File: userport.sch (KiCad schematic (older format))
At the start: 25 parts, among them CN10 USERPORT, U122 74LS654, U21 74HCT04, U22 MOS_6529, U23 MOS_6551_ACIA, U28 GAL16V8, Y2 1.8432M

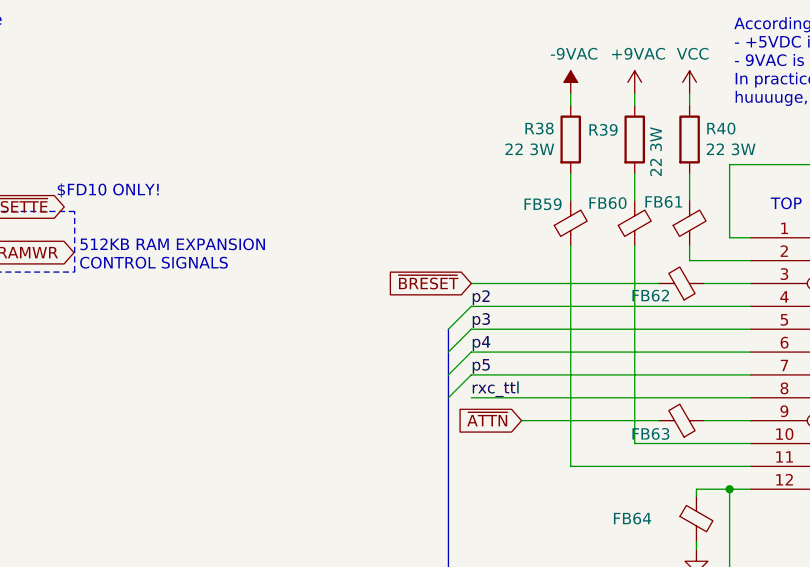
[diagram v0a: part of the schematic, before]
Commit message: Replace /BRESET on Expansion Port and User Port with /RESET This was an oversight we probably introduced in V3 which makes it impossible for the Expansion Port and User Port to reset the machine through the RESET pin. The /BRESET line only went to the IEC Port in the original machine, which means that "Serial button dongles" cannot reset the machine, unlike on the C64. Maybe we should introduce a jumper for that?
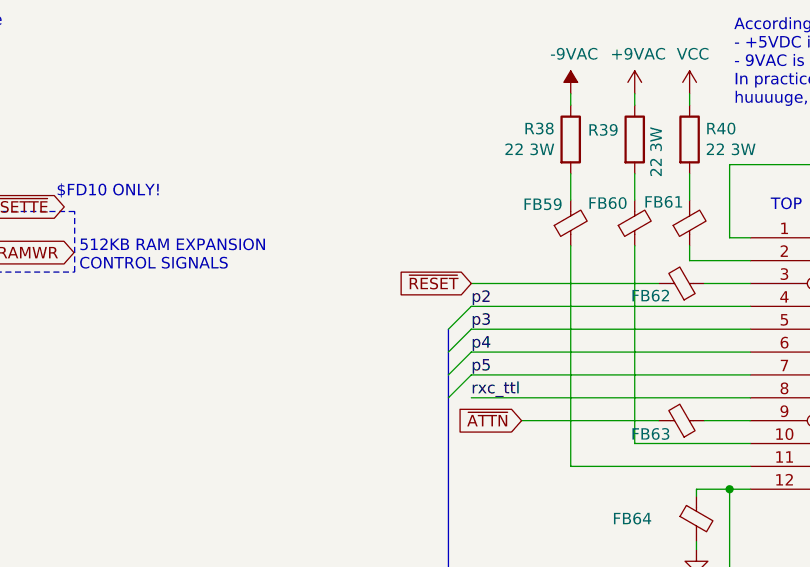
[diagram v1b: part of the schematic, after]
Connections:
- net ~BRESET is gone; now on net ~RESET: FB62.2
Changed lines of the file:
@@
 Sheet 13 14
 Title "LittleSixteen"
-Date "2023-02-14"
+Date "2024-07-21"
 Rev "4git"
 Comp "SukkoPera"
@@
 	2910 3125 2910 3365
 Text GLabel 6470 6730 0    50   Input ~ 0
-~BRESET
+~RESET
 $Comp
 L 74xx:74LS04 U21

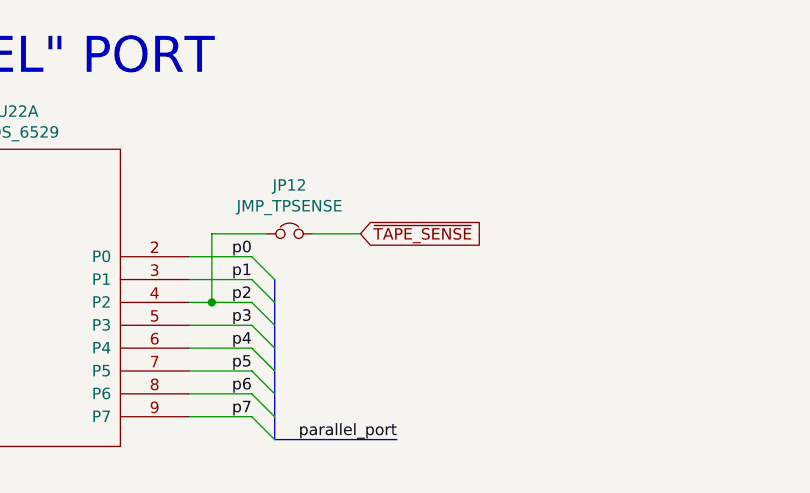
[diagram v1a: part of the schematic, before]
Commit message: Add P7 option for Tape Sense jumper, in order to replicate Plus/4 J8/J9
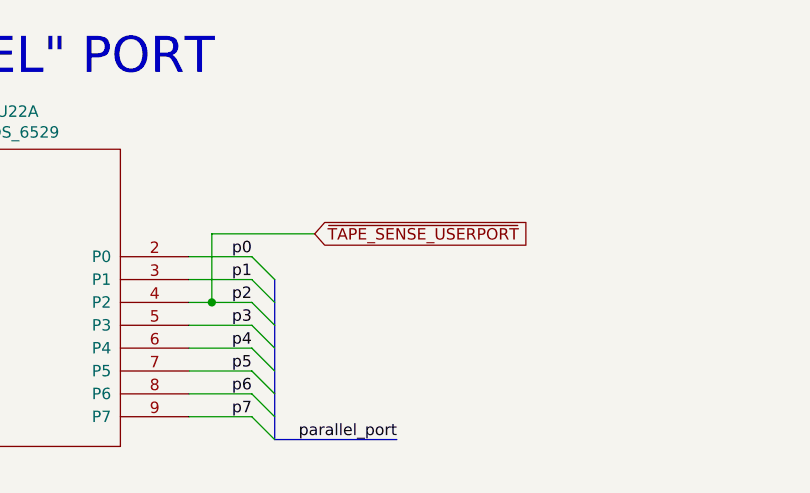
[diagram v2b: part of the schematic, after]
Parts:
- removed JP12: JMP_TPSENSE, Connector_PinHeader_2.54mm:PinHeader_1x02_P2.54mm_Vertical, symbol Device:Jumper_NC_Small
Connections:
- net p2 renamed ~TAPE_SENSE_USERPORT
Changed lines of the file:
@@
 Sheet 13 14
 Title "LittleSixteen"
-Date "2024-07-21"
+Date "2024-08-07"
 Rev "4git"
 Comp "SukkoPera"
@@
 Text GLabel 11775 1380 0    50   Input ~ 0
 R_~W
-Wire Wire Line
-	14150 1520 13940 1520
-$Comp
-L Device:Jumper_NC_Small JP?
-U 1 1 6486FE58
-P 13840 1520
-AR Path="/5E6A379E/6486FE58" Ref="JP?"  Part="1"
-AR Path="/63EAD078/6486FE58" Ref="JP12"  Part="1"
-F 0 "JP12" H 13840 1732 50  0000 C CNN
-F 1 "JMP_TPSENSE" H 13840 1641 50  0000 C CNN
-F 2 "Connector_PinHeader_2.54mm:PinHeader_1x02_P2.54mm_Vertical" H 13840 1520 50  0001 C CNN
-F 3 "~" H 13840 1520 50  0001 C CNN
-	1    13840 1520
-	-1   0    0    -1
-$EndComp
-Text GLabel 14150 1520 2    50   Input ~ 0
-~TAPE_SENSE
 $Comp
 L emi_filter_3pin:EMI_Filter_3Pin FB?
@@
 Wire Wire Line
 	13500 1520 13500 1820
-Wire Wire Line
-	13500 1520 13740 1520
 Connection ~ 13500 1820
 Wire Wire Line
@@
 Text Notes 1380 5695 0    50   ~ 0
 Generates:\n- Control signals for the Hannes RAM Expansion register at $FD16\n- ~CS~ for the User Port MOS 6529 (or replacement) at $FD10 only, named ~CASSETTE~ here\n- Other control signals for the User Port MOS 6529 replacement circuit
+Text GLabel 13950 1520 2    50   Input ~ 0
+~TAPE_SENSE_USERPORT
+Wire Wire Line
+	13500 1520 13950 1520
 Wire Bus Line
 	9765 6730 9765 8260

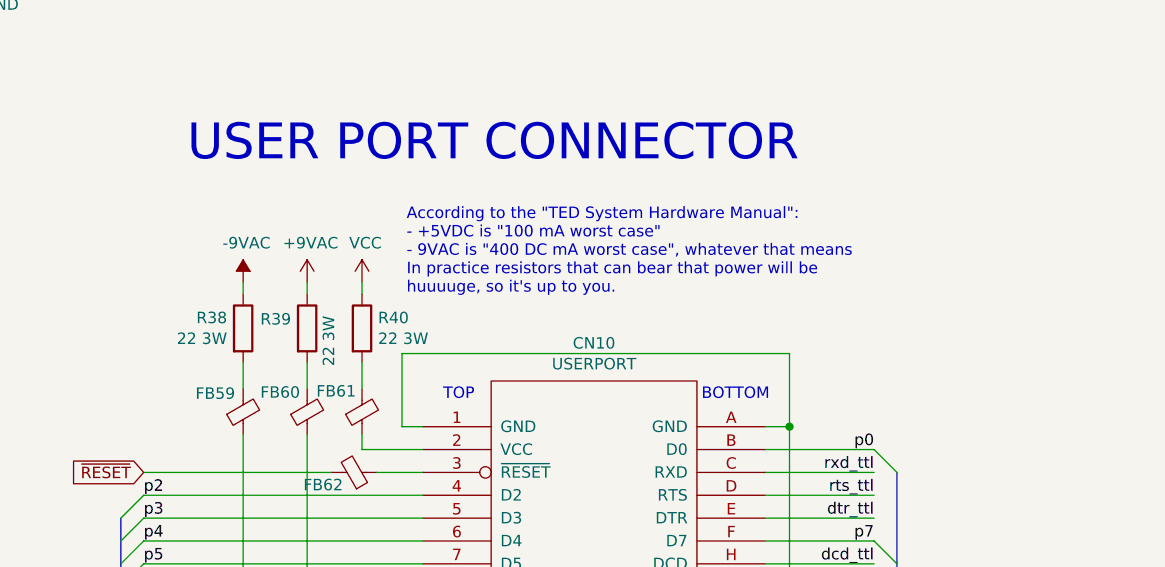
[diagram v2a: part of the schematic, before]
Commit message: Switch to polyfuses on userport and to ferrites for FB38/39/40
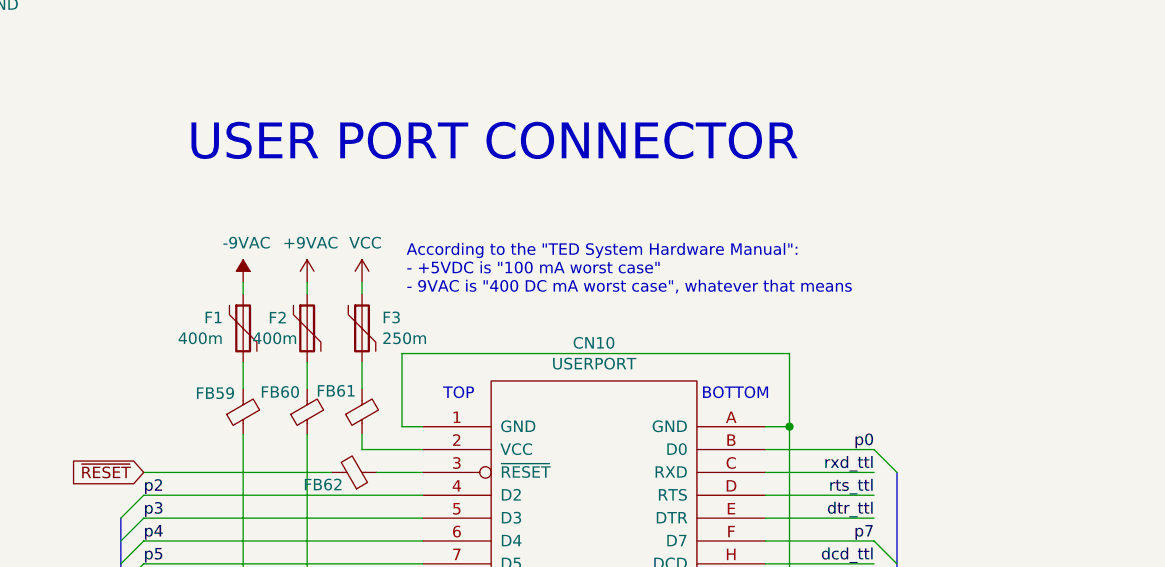
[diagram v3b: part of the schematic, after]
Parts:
- removed R38, R39, R40: 22 3W, Resistor_THT:R_Axial_DIN0414_L11.9mm_D4.5mm_P5.08mm_Vertical, symbol Device:R
- added F1, F2: 400m, Fuse:Fuse_Bourns_MF-RG400, symbol Device:Polyfuse
- added F3: 250m, Fuse:Fuse_Bourns_MF-RG400, symbol Device:Polyfuse
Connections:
- net +9VAC: now also F2.1
- net -9VAC: now also F1.1
- net VCC: now also F3.1
- net at FB60.2: now also F2.2
- net at FB61.2: now also F3.2
- net at FB59.2: now also F1.2
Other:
- note added: "According to the "TED System Hardware Manual":\n- +5VDC is "100 mA worst case"\n- 9VAC is "400 DC mA worst case", whatever that means\n"
- note removed: "According to the "TED System Hardware Manual":\n- +5VDC is "100 mA worst case"\n- 9VAC is "400 DC mA worst case", whatever that means\nIn practice resistors that can bear that power will be\nhuuuuge, so it's up to you."
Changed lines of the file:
@@
 Sheet 13 14
 Title "LittleSixteen"
-Date "2024-08-07"
+Date "2025-01-04"
 Rev "4git"
 Comp "SukkoPera"
@@
 	1    0    0    1
 $EndComp
-$Comp
-L Device:R R?
-U 1 1 647C5CFF
-P 7425 6100
-AR Path="/61BCD018/647C5CFF" Ref="R?"  Part="1"
-AR Path="/5ECB474B/647C5CFF" Ref="R?"  Part="1"
-AR Path="/63EAD078/647C5CFF" Ref="R40"  Part="1"
-F 0 "R40" H 7495 6146 50  0000 L CNN
-F 1 "22 3W" H 7495 6055 50  0000 L CNN
-F 2 "Resistor_THT:R_Axial_DIN0414_L11.9mm_D4.5mm_P5.08mm_Vertical" V 7355 6100 50  0001 C CNN
-F 3 "~" H 7425 6100 50  0001 C CNN
-	1    7425 6100
-	1    0    0    -1
-$EndComp
 Wire Wire Line
 	7425 5950 7425 5900
@@
 Wire Wire Line
 	13500 1820 13675 1820
-$Comp
-L Device:R R?
-U 1 1 64956DD2
-P 6905 6100
-AR Path="/61BCD018/64956DD2" Ref="R?"  Part="1"
-AR Path="/5ECB474B/64956DD2" Ref="R?"  Part="1"
-AR Path="/63EAD078/64956DD2" Ref="R38"  Part="1"
-F 0 "R38" H 6835 6146 50  0000 R CNN
-F 1 "22 3W" H 6835 6055 50  0000 R CNN
-F 2 "Resistor_THT:R_Axial_DIN0414_L11.9mm_D4.5mm_P5.08mm_Vertical" V 6835 6100 50  0001 C CNN
-F 3 "~" H 6905 6100 50  0001 C CNN
-	1    6905 6100
-	1    0    0    -1
-$EndComp
 Wire Wire Line
 	6905 5950 6905 5900
@@
 	7185 6250 7185 6365
 Text Notes 7620 5955 0    50   ~ 0
-According to the "TED System Hardware Manual":\n- +5VDC is "100 mA worst case"\n- 9VAC is "400 DC mA worst case", whatever that means\nIn practice resistors that can bear that power will be\nhuuuuge, so it's up to you.
-$Comp
-L Device:R R?
-U 1 1 64956726
-P 7185 6100
-AR Path="/61BCD018/64956726" Ref="R?"  Part="1"
-AR Path="/5ECB474B/64956726" Ref="R?"  Part="1"
-AR Path="/63EAD078/64956726" Ref="R39"  Part="1"
-F 0 "R39" H 6980 6140 50  0000 L CNN
-F 1 "22 3W" V 7280 5935 50  0000 L CNN
-F 2 "Resistor_THT:R_Axial_DIN0414_L11.9mm_D4.5mm_P5.08mm_Vertical" V 7115 6100 50  0001 C CNN
-F 3 "~" H 7185 6100 50  0001 C CNN
-	1    7185 6100
-	1    0    0    -1
-$EndComp
+According to the "TED System Hardware Manual":\n- +5VDC is "100 mA worst case"\n- 9VAC is "400 DC mA worst case", whatever that means\n
 Wire Wire Line
 	7600 6530 7600 6210
@@
 Wire Bus Line
 	1695 6195 1695 7095
+$Comp
+L Device:Polyfuse F3
+U 1 1 677AFD86
+P 7425 6100
+F 0 "F3" H 7513 6146 50  0000 L CNN
+F 1 "250m" H 7513 6055 50  0000 L CNN
+F 2 "Fuse:Fuse_Bourns_MF-RG400" H 7475 5900 50  0001 L CNN
+F 3 "~" H 7425 6100 50  0001 C CNN
+F 4 " 603-BK60-025-DZ" H 7425 6100 50  0001 C CNN "MouserPN"
+	1    7425 6100
+	1    0    0    -1
+$EndComp
+$Comp
+L Device:Polyfuse F1
+U 1 1 677B0E80
+P 6905 6100
+F 0 "F1" H 6817 6146 50  0000 R CNN
+F 1 "400m" H 6817 6055 50  0000 R CNN
+F 2 "Fuse:Fuse_Bourns_MF-RG400" H 6955 5900 50  0001 L CNN
+F 3 "~" H 6905 6100 50  0001 C CNN
+F 4 " 603-BK60-040-DI" H 6905 6100 50  0001 C CNN "MouserPN"
+	1    6905 6100
+	1    0    0    -1
+$EndComp
+$Comp
+L Device:Polyfuse F2
+U 1 1 677B15C8
+P 7185 6100
+F 0 "F2" H 7015 6145 50  0000 L CNN
+F 1 "400m" H 6945 6055 50  0000 L CNN
+F 2 "Fuse:Fuse_Bourns_MF-RG400" H 7235 5900 50  0001 L CNN
+F 3 "~" H 7185 6100 50  0001 C CNN
+F 4 " 603-BK60-040-DI" H 7185 6100 50  0001 C CNN "MouserPN"
+	1    7185 6100
+	1    0    0    -1
+$EndComp
 $EndSCHEMATC

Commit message: Fix some P/Ns
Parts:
- F1, F2: MouserPN 603-BK60-040-DI -> 603-BK60-040-DI
- F3: MouserPN 603-BK60-025-DZ -> 603-BK60-025-DZ
- FB59, FB60, FB61, FB62, FB63, FB64, FB65: value DSS1NB32A271Q91A -> FERRITE; MouserPN (none) -> 623-2743015112
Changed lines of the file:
@@
 AR Path="/63EAD078/647718B2" Ref="FB62"  Part="1"
 F 0 "FB62" V 7335 6595 50  0000 C CNN
-F 1 "DSS1NB32A271Q91A" H 7490 6685 50  0001 L CNN
+F 1 "FERRITE" H 7490 6685 50  0001 L CNN
 F 2 "LittleSixteen:EMI_Filter" V 7320 6730 50  0001 C CNN
 F 3 "~" H 7390 6730 50  0001 C CNN
+F 4 "623-2743015112" H 7390 6730 50  0001 C CNN "MouserPN"
 	1    7390 6730
 	0    1    -1   0
@@
 AR Path="/63EAD078/6477BD12" Ref="FB60"  Part="1"
 F 0 "FB60" H 6980 6380 50  0000 L CNN
-F 1 "DSS1NB32A271Q91A" H 7285 6420 50  0001 L CNN
+F 1 "FERRITE" H 7285 6420 50  0001 L CNN
 F 2 "LittleSixteen:EMI_Filter" V 7115 6465 50  0001 C CNN
 F 3 "~" H 7185 6465 50  0001 C CNN
+F 4 "623-2743015112" H 7185 6465 50  0001 C CNN "MouserPN"
 	1    7185 6465
 	1    0    0    1
@@
 AR Path="/63EAD078/64790452" Ref="FB64"  Part="1"
 F 0 "FB64" H 7261 7760 50  0000 R CNN
-F 1 "DSS1NB32A271Q91A" H 7555 7715 50  0001 L CNN
+F 1 "FERRITE" H 7555 7715 50  0001 L CNN
 F 2 "LittleSixteen:EMI_Filter" V 7385 7760 50  0001 C CNN
 F 3 "~" H 7455 7760 50  0001 C CNN
+F 4 "623-2743015112" H 7455 7760 50  0001 C CNN "MouserPN"
 	1    7455 7760
 	1    0    0    -1
@@
 AR Path="/63EAD078/647AEC6A" Ref="FB65"  Part="1"
 F 0 "FB65" H 9050 7685 50  0000 L CNN
-F 1 "DSS1NB32A271Q91A" H 9395 7715 50  0001 L CNN
+F 1 "FERRITE" H 9395 7715 50  0001 L CNN
 F 2 "LittleSixteen:EMI_Filter" V 9225 7760 50  0001 C CNN
 F 3 "~" H 9295 7760 50  0001 C CNN
+F 4 "623-2743015112" H 9295 7760 50  0001 C CNN "MouserPN"
 	1    9295 7760
 	1    0    0    -1
@@
 AR Path="/63EAD078/647B8E58" Ref="FB61"  Part="1"
 F 0 "FB61" H 7225 6375 50  0000 L CNN
-F 1 "DSS1NB32A271Q91A" H 7525 6420 50  0001 L CNN
+F 1 "FERRITE" H 7525 6420 50  0001 L CNN
 F 2 "LittleSixteen:EMI_Filter" V 7355 6465 50  0001 C CNN
 F 3 "~" H 7425 6465 50  0001 C CNN
+F 4 "623-2743015112" H 7425 6465 50  0001 C CNN "MouserPN"
 	1    7425 6465
 	1    0    0    1
@@
 AR Path="/63EAD078/6479A5EF" Ref="FB63"  Part="1"
 F 0 "FB63" V 7330 7195 50  0000 C CNN
-F 1 "DSS1NB32A271Q91A" H 7490 7285 50  0001 L CNN
+F 1 "FERRITE" H 7490 7285 50  0001 L CNN
 F 2 "LittleSixteen:EMI_Filter" V 7320 7330 50  0001 C CNN
 F 3 "~" H 7390 7330 50  0001 C CNN
+F 4 "623-2743015112" H 7390 7330 50  0001 C CNN "MouserPN"
 	1    7390 7330
 	0    1    -1   0
@@
 AR Path="/63EAD078/647EB007" Ref="FB59"  Part="1"
 F 0 "FB59" H 6870 6385 50  0000 R CNN
-F 1 "DSS1NB32A271Q91A" H 7005 6420 50  0001 L CNN
+F 1 "FERRITE" H 7005 6420 50  0001 L CNN
 F 2 "LittleSixteen:EMI_Filter" V 6835 6465 50  0001 C CNN
 F 3 "~" H 6905 6465 50  0001 C CNN
+F 4 "623-2743015112" H 6905 6465 50  0001 C CNN "MouserPN"
 	1    6905 6465
 	1    0    0    1
@@
 Wire Wire Line
 	13500 1520 13950 1520
-Wire Bus Line
-	9765 6730 9765 8260
-Wire Bus Line
-	6370 6930 6370 8260
-Wire Bus Line
-	11525 1720 11525 2420
-Wire Bus Line
-	15210 4455 15210 5155
-Wire Bus Line
-	11525 4555 11525 5255
-Wire Bus Line
-	13775 1720 13775 2420
-Wire Bus Line
-	6130 2525 6130 3225
-Wire Bus Line
-	1695 6195 1695 7095
 $Comp
 L Device:Polyfuse F3
@@
 F 2 "Fuse:Fuse_Bourns_MF-RG400" H 7475 5900 50  0001 L CNN
 F 3 "~" H 7425 6100 50  0001 C CNN
-F 4 " 603-BK60-025-DZ" H 7425 6100 50  0001 C CNN "MouserPN"
+F 4 "603-BK60-025-DZ" H 7425 6100 50  0001 C CNN "MouserPN"
 	1    7425 6100
 	1    0    0    -1
@@
 F 2 "Fuse:Fuse_Bourns_MF-RG400" H 6955 5900 50  0001 L CNN
 F 3 "~" H 6905 6100 50  0001 C CNN
-F 4 " 603-BK60-040-DI" H 6905 6100 50  0001 C CNN "MouserPN"
+F 4 "603-BK60-040-DI" H 6905 6100 50  0001 C CNN "MouserPN"
 	1    6905 6100
 	1    0    0    -1
@@
 F 2 "Fuse:Fuse_Bourns_MF-RG400" H 7235 5900 50  0001 L CNN
 F 3 "~" H 7185 6100 50  0001 C CNN
-F 4 " 603-BK60-040-DI" H 7185 6100 50  0001 C CNN "MouserPN"
+F 4 "603-BK60-040-DI" H 7185 6100 50  0001 C CNN "MouserPN"
 	1    7185 6100
 	1    0    0    -1
 $EndComp
+Wire Bus Line
+	9765 6730 9765 8260
+Wire Bus Line
+	6370 6930 6370 8260
+Wire Bus Line
+	11525 1720 11525 2420
+Wire Bus Line
+	15210 4455 15210 5155
+Wire Bus Line
+	11525 4555 11525 5255
+Wire Bus Line
+	13775 1720 13775 2420
+Wire Bus Line
+	6130 2525 6130 3225
+Wire Bus Line
+	1695 6195 1695 7095
 $EndSCHEMATC

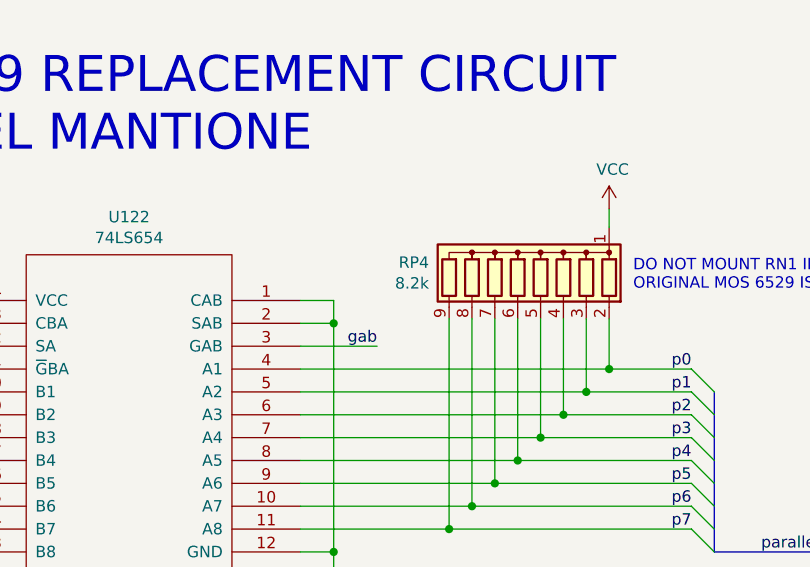
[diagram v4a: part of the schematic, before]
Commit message: RP4 -> 3.3k Thanks @gordonfpanam!
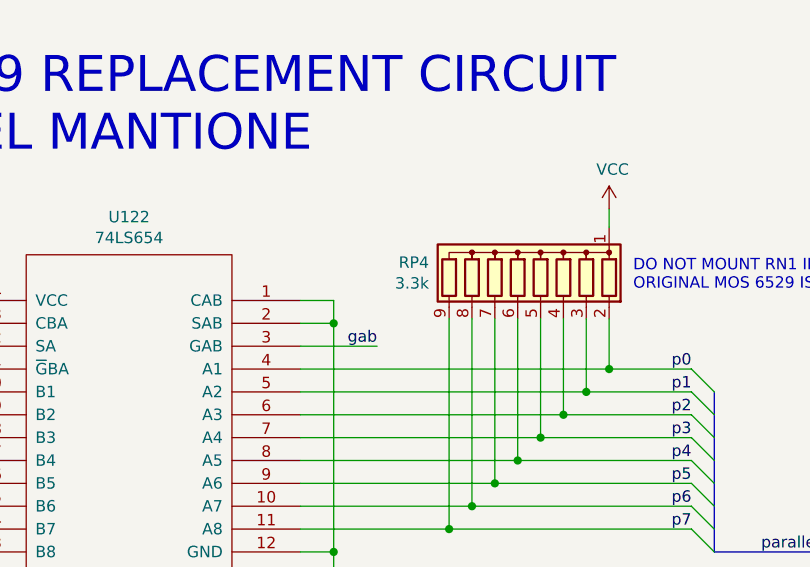
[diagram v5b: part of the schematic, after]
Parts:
- RP4: value 8.2k -> 3.3k
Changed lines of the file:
@@
 Sheet 13 14
 Title "LittleSixteen"
-Date "2025-01-04"
+Date "2025-06-22"
 Rev "4git"
 Comp "SukkoPera"
@@
 P 14350 3935
 F 0 "RP4" H 14738 3981 50  0000 L CNN
-F 1 "8.2k" H 14738 3890 50  0000 L CNN
+F 1 "3.3k" H 14738 3890 50  0000 L CNN
 F 2 "Resistor_THT:R_Array_SIP9" V 14825 3935 50  0001 C CNN
 F 3 "http://www.vishay.com/docs/31509/csc.pdf" H 14350 3935 50  0001 C CNN
